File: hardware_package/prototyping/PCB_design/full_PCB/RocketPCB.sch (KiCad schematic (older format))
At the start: 67 parts, among them J1 USB_C_Receptacle, J2 Micro_SD_Card, J3 Conn_01x03_Female, Q1 DMG2301L, SW1 SW_Push, SW2 SW_Push, U1 STM32F405RGTx, U2 TPS62160DSG, U3 RFM69HCW, U4 MPU-6050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

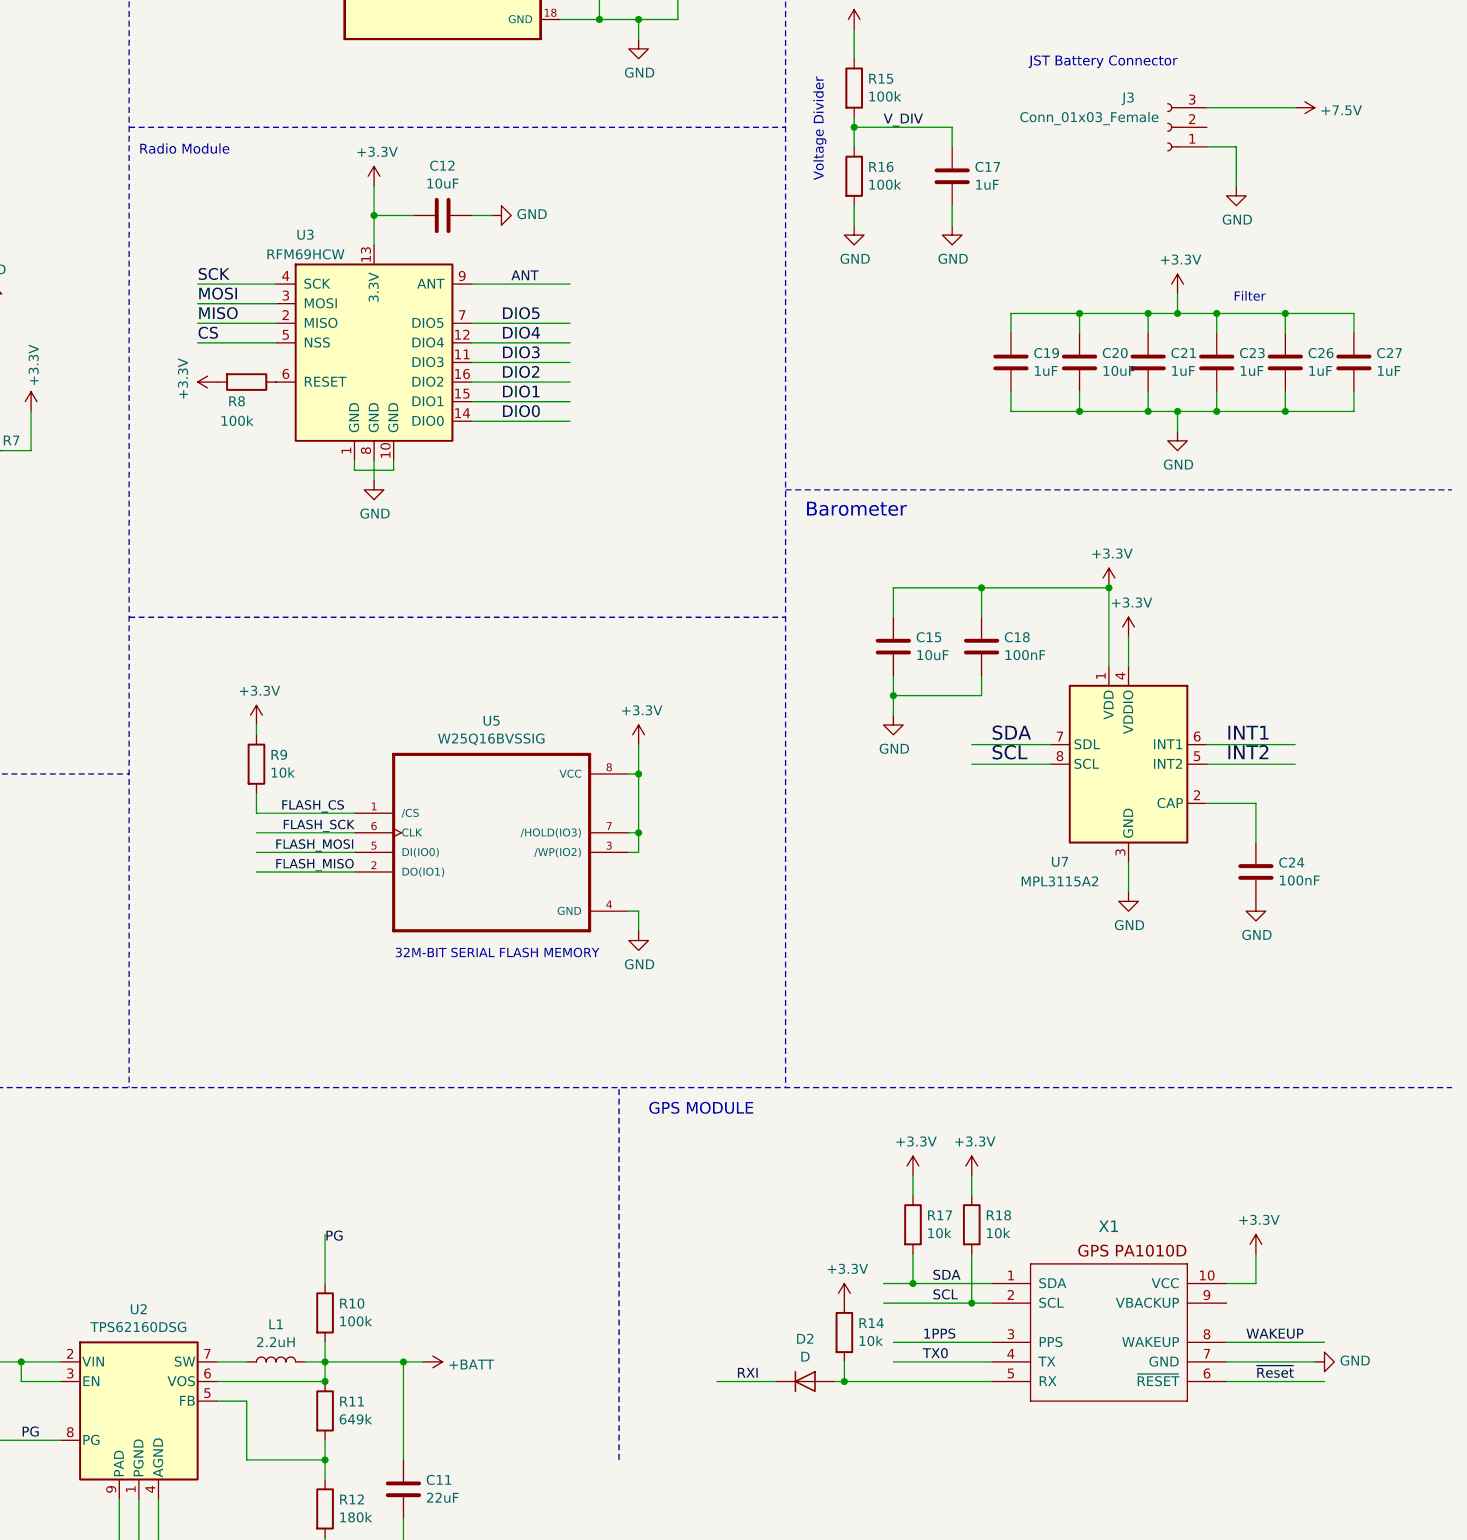
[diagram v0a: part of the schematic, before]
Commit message: Assigned additional footprints adding headers for radio and GPS
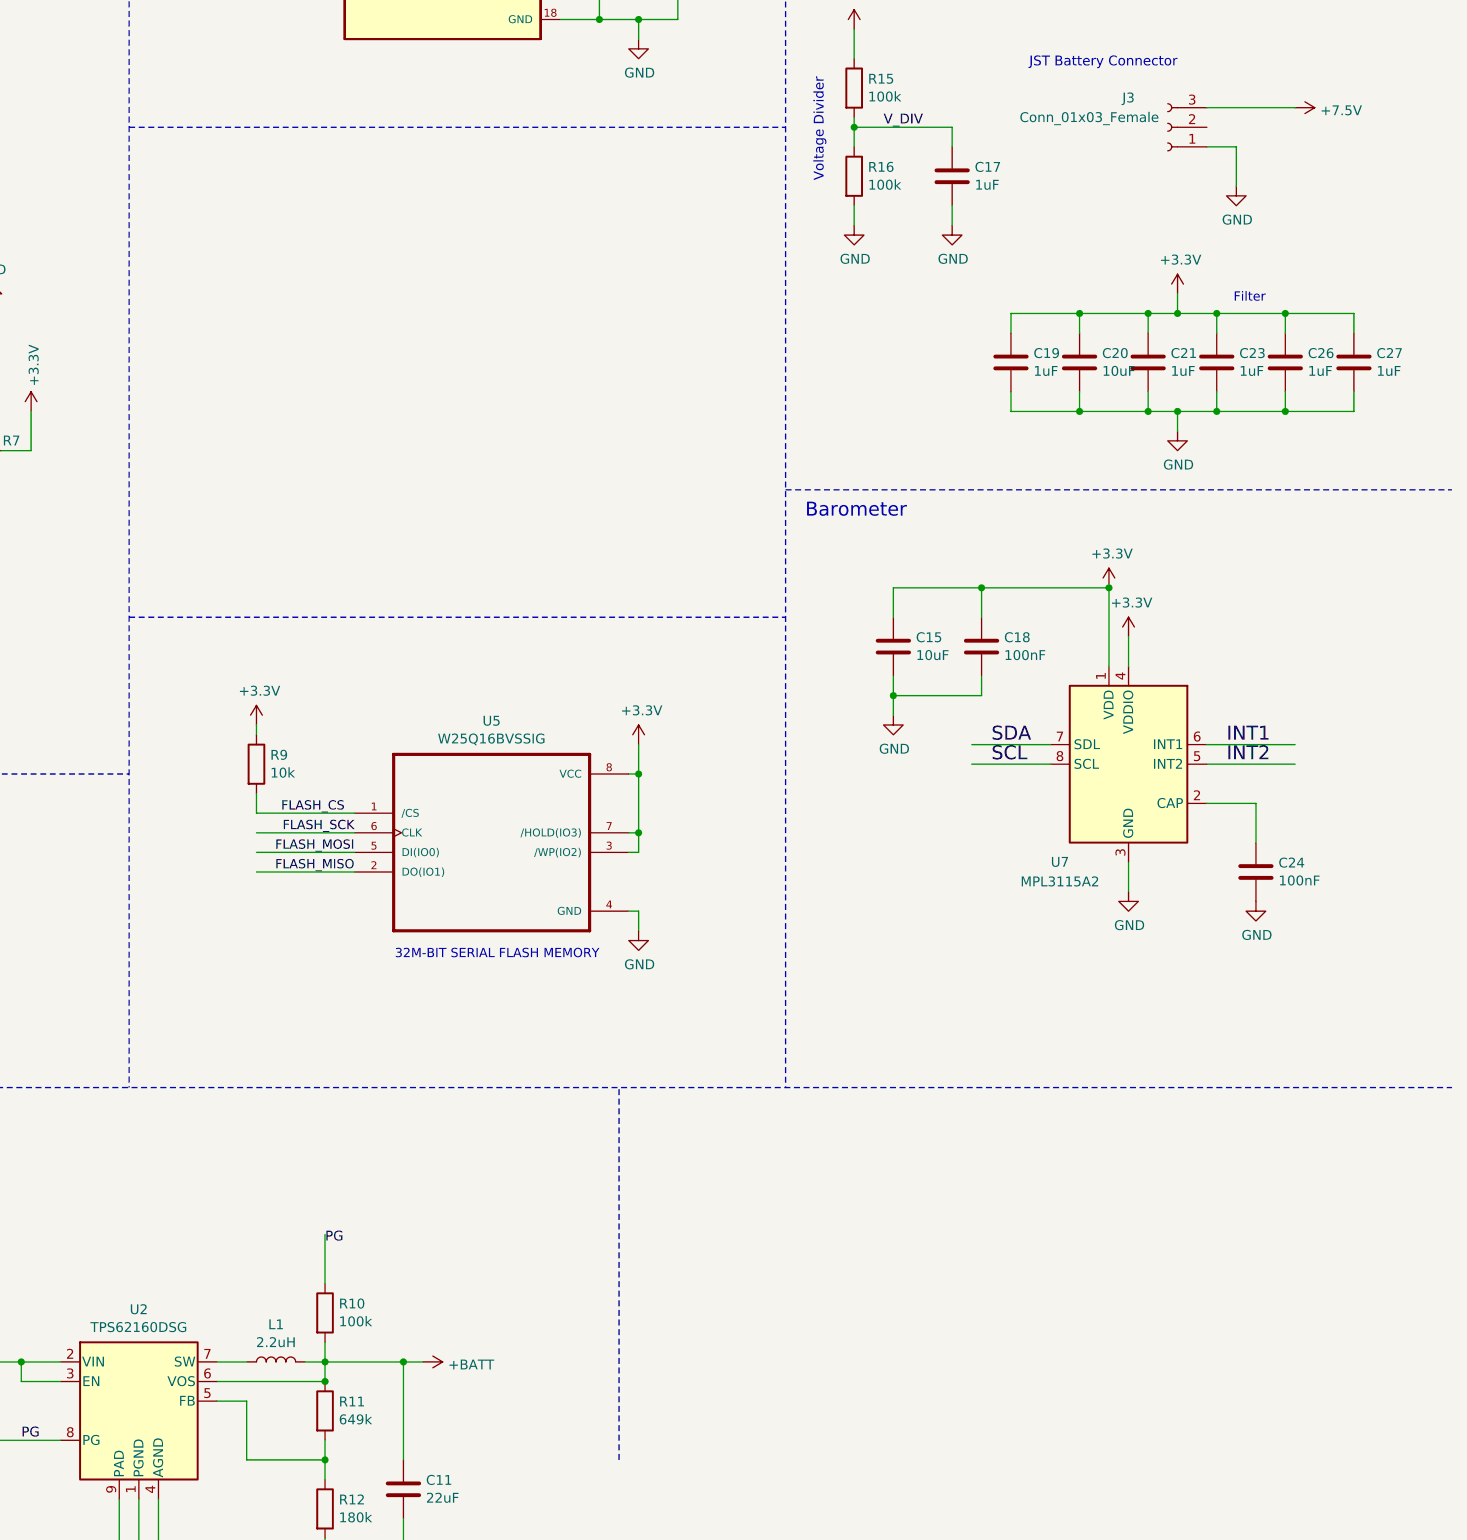
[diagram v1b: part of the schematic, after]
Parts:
- removed C12: 10uF, Capacitor_THT:CP_Radial_D5.0mm_P2.50mm, symbol Device:C
- removed D2: D, LED_THT:LED_D5.0mm_Clear, symbol Device:D
- removed R14, R17, R18: 10k, Resistor_THT:R_Axial_DIN0207_L6.3mm_D2.5mm_P7.62mm_Horizontal, symbol Device:R
- removed R8: 100k, Resistor_THT:R_Axial_DIN0207_L6.3mm_D2.5mm_P7.62mm_Horizontal, symbol Device:R
- removed U3: RFM69HCW, symbol RocketPCB-rescue:RFM69HCW-RF_AM_FM
- removed X1: GPS_PA1010D, symbol RocketPCB-rescue:GPS_PA1010D-gps_pa1010d
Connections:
- net labels removed: 1PPS, ANT, DIO0, DIO1, DIO2, DIO3, DIO4, DIO5, RXI, TX0, WAKEUP, ~Reset~
- wire segments 321 -> 283
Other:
- note removed: "GPS MODULE\n"
- note removed: "Radio Module"

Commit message: Added all FPs some issues still, +safety features and regulator
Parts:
- removed U5: W25Q16BVSSIG, symbol RocketPCB-rescue:W25Q16BVSSIG-W25Q16BVSSIG
- added C12, C28: 10uF, Capacitor_THT:CP_Radial_D5.0mm_P2.50mm, symbol Device:C
- added C29: 0.1uF, Capacitor_THT:CP_Radial_D5.0mm_P2.50mm, symbol Device:C
- added C30: 10pF, Capacitor_THT:CP_Radial_D5.0mm_P2.50mm, symbol Device:C
- added C31, C32, C33: 22uF, Capacitor_THT:CP_Radial_D5.0mm_P2.50mm, symbol Device:C
- added F1: Polyfuse, Fuse:Fuse_Littelfuse_395Series, symbol Device:Polyfuse
- added L2: 1uH, Inductor_THT:L_Axial_L9.5mm_D4.0mm_P12.70mm_Horizontal_Fastron_SMCC, symbol Device:L
- added Q2: Q_PMOS_DGS, Package_TO_SOT_SMD:SOT-23, symbol Device:Q_PMOS_DGS
- added R14: 1M, Resistor_THT:R_Axial_DIN0204_L3.6mm_D1.6mm_P7.62mm_Horizontal, symbol Device:R
- added R8: 2.2M, Resistor_THT:R_Axial_DIN0204_L3.6mm_D1.6mm_P7.62mm_Horizontal, symbol Device:R
- added U3: Radio_Header, GPS_head0:gps_header_footprint, symbol radio_header:Radio_Header
- added U5: W25Q16JV, GPS_head0:W25Q16JV_footprint, symbol flash_memory:W25Q16JV
- added U8: GPS_header, GPS_head0:GPS_header_fp, symbol gps_header:GPS_header
- added U9: TPS63060, Package_SON:Texas_S-PWSON-N10_ThermalVias, symbol Regulator_Switching:TPS63060
- R9: value 10k -> 200k; footprint Resistor_THT:R_Axial_DIN0207_L6.3mm_D2.5mm_P7.62mm_Horizontal -> Resistor_THT:R_Axial_DIN0204_L3.6mm_D1.6mm_P7.62mm_Horizontal
- U4: footprint (none) -> GPS_head0:MPU6050-footprint
- Y1: footprint (none) -> Oscillator:Oscillator_DIP-14_LargePads
- Y2: value 32.768 -> 32MHz; footprint (none) -> Oscillator:Oscillator_DIP-8_LargePads
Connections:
- net labels added: +6V, G0, PPS, RXI, TX0
- wire segments 283 -> 370
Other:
- note added: "16M-BIT SERIAL FLASH MEMORY"
- note added: "3.7V out"
- note added: "FLASH MEMORY\n"
- note added: "GPS Module"
- note added: "Radio Module\n"
- note added: "Voltage Regulator Servos - 6V\n"
- note removed: "32M-BIT SERIAL FLASH MEMORY"
- moved on the sheet: J3

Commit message: Begun laying out PCB
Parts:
- Q2: footprint Package_TO_SOT_SMD:SOT-23 -> (none)
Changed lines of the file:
@@
 Wire Wire Line
 	1650 6900 1850 6900
-Wire Wire Line
-	1650 6900 1050 6900
 Connection ~ 1650 6900
 $Comp
@@
 $EndComp
 $Comp
-L Device:C C12
-U 1 1 5FAE0189
-P 900 7900
-F 0 "C12" H 700 8050 50  0000 L CNN
-F 1 "10uF" H 650 7800 50  0000 L CNN
-F 2 "Capacitor_THT:CP_Radial_D5.0mm_P2.50mm" H 938 7750 50  0001 C CNN
-F 3 "~" H 900 7900 50  0001 C CNN
-	1    900  7900
-	1    0    0    -1
-$EndComp
-$Comp
-L Device:C C28
-U 1 1 5FAE6549
-P 1150 7900
-F 0 "C28" H 1265 7946 50  0000 L CNN
-F 1 "10uF" H 1265 7855 50  0000 L CNN
-F 2 "Capacitor_THT:CP_Radial_D5.0mm_P2.50mm" H 1188 7750 50  0001 C CNN
-F 3 "~" H 1150 7900 50  0001 C CNN
-	1    1150 7900
-	1    0    0    -1
-$EndComp
-Wire Wire Line
-	1050 6900 1050 7550
-Wire Wire Line
-	1050 7550 1150 7550
-Wire Wire Line
-	1150 7550 1150 7750
-Connection ~ 1050 6900
-Wire Wire Line
-	1050 6900 950  6900
-Wire Wire Line
-	1050 7550 900  7550
-Wire Wire Line
-	900  7550 900  7750
-Connection ~ 1050 7550
-$Comp
-L power:GND #PWR0112
-U 1 1 5FB20758
-P 1000 8200
-F 0 "#PWR0112" H 1000 7950 50  0001 C CNN
-F 1 "GND" V 1005 8072 50  0000 R CNN
-F 2 "" H 1000 8200 50  0001 C CNN
-F 3 "" H 1000 8200 50  0001 C CNN
-	1    1000 8200
-	1    0    0    -1
-$EndComp
-Wire Wire Line
-	900  8050 900  8200
-Wire Wire Line
-	900  8200 1000 8200
-Wire Wire Line
-	1000 8200 1150 8200
-Wire Wire Line
-	1150 8200 1150 8050
-Connection ~ 1000 8200
-$Comp
 L Device:C C29
 U 1 1 5FBBFED9
@@
 Wire Wire Line
 	3700 6900 3700 7300
-$Comp
-L Device:C C31
-U 1 1 5FE129F8
-P 4050 7250
-F 0 "C31" H 4165 7296 50  0000 L CNN
-F 1 "22uF" H 4150 7200 50  0000 L CNN
-F 2 "Capacitor_THT:CP_Radial_D5.0mm_P2.50mm" H 4088 7100 50  0001 C CNN
-F 3 "~" H 4050 7250 50  0001 C CNN
-	1    4050 7250
-	1    0    0    -1
-$EndComp
-$Comp
-L Device:C C32
-U 1 1 5FE133D9
-P 4450 7250
-F 0 "C32" H 4565 7296 50  0000 L CNN
-F 1 "22uF" H 4550 7200 50  0000 L CNN
-F 2 "Capacitor_THT:CP_Radial_D5.0mm_P2.50mm" H 4488 7100 50  0001 C CNN
-F 3 "~" H 4450 7250 50  0001 C CNN
-	1    4450 7250
-	1    0    0    -1
-$EndComp
-$Comp
-L Device:C C33
-U 1 1 5FE138A3
-P 4850 7250
-F 0 "C33" H 4965 7296 50  0000 L CNN
-F 1 "22uF" H 4950 7200 50  0000 L CNN
-F 2 "Capacitor_THT:CP_Radial_D5.0mm_P2.50mm" H 4888 7100 50  0001 C CNN
-F 3 "~" H 4850 7250 50  0001 C CNN
-	1    4850 7250
-	1    0    0    -1
-$EndComp
-Wire Wire Line
-	4050 7400 4050 7550
-Wire Wire Line
-	4050 7550 4450 7550
-Wire Wire Line
-	4450 7550 4450 7400
-Wire Wire Line
-	4850 7400 4850 7550
-Wire Wire Line
-	4850 7550 4450 7550
-Connection ~ 4450 7550
-$Comp
-L power:GND #PWR0115
-U 1 1 5FE60576
-P 4450 7650
-F 0 "#PWR0115" H 4450 7400 50  0001 C CNN
-F 1 "GND" V 4455 7522 50  0000 R CNN
-F 2 "" H 4450 7650 50  0001 C CNN
-F 3 "" H 4450 7650 50  0001 C CNN
-	1    4450 7650
-	1    0    0    -1
-$EndComp
-Wire Wire Line
-	4450 7550 4450 7650
 Wire Wire Line
 	3700 6900 4050 6900
-Wire Wire Line
-	4850 6900 4850 7100
 Connection ~ 3700 6900
-Wire Wire Line
-	4450 6900 4450 7100
-Connection ~ 4450 6900
-Wire Wire Line
-	4450 6900 4850 6900
 Wire Wire Line
 	4050 6900 4050 7100
 Connection ~ 4050 6900
 Wire Wire Line
-	4050 6900 4450 6900
-Wire Wire Line
 	2650 6900 3050 6900
 Wire Wire Line
@@
 Wire Wire Line
 	2850 7250 3050 7250
-Wire Wire Line
-	4850 6900 5200 6900
-Connection ~ 4850 6900
 $Comp
 L power:+6V #PWR0116
@@
 Text Notes 600  5400 0    71   ~ 0
 Voltage Regulator Servos - 6V\n
-$Comp
-L Device:Q_PMOS_DGS Q2
-U 1 1 6006F0DB
-P 14950 2650
-F 0 "Q2" V 15292 2650 50  0000 C CNN
-F 1 "Q_PMOS_DGS" V 15201 2650 50  0000 C CNN
-F 2 "Package_TO_SOT_SMD:SOT-23" H 15150 2750 50  0001 C CNN
-F 3 "~" H 14950 2650 50  0001 C CNN
-	1    14950 2650
-	0    -1   -1   0
-$EndComp
 Wire Wire Line
 	14450 2900 14950 2900
@@
 Wire Wire Line
 	15600 2550 15650 2550
+Wire Wire Line
+	4050 7400 4050 7550
+Wire Wire Line
+	4050 7550 4450 7550
+Wire Wire Line
+	4450 7550 4450 7650
+$Comp
+L power:GND #PWR0115
+U 1 1 5FE60576
+P 4450 7650
+F 0 "#PWR0115" H 4450 7400 50  0001 C CNN
+F 1 "GND" V 4455 7522 50  0000 R CNN
+F 2 "" H 4450 7650 50  0001 C CNN
+F 3 "" H 4450 7650 50  0001 C CNN
+	1    4450 7650
+	1    0    0    -1
+$EndComp
+$Comp
+L Device:C C31
+U 1 1 5FE129F8
+P 4050 7250
+F 0 "C31" H 4165 7296 50  0000 L CNN
+F 1 "22uF" H 4150 7200 50  0000 L CNN
+F 2 "Capacitor_THT:CP_Radial_D5.0mm_P2.50mm" H 4088 7100 50  0001 C CNN
+F 3 "~" H 4050 7250 50  0001 C CNN
+	1    4050 7250
+	1    0    0    -1
+$EndComp
+Wire Wire Line
+	4050 6900 4450 6900
+Connection ~ 4450 6900
+Wire Wire Line
+	4450 6900 4450 7100
+Connection ~ 4450 7550
+Wire Wire Line
+	4450 7550 4450 7400
+Wire Wire Line
+	4850 7550 4450 7550
+Wire Wire Line
+	4850 6900 5200 6900
+Wire Wire Line
+	4450 6900 4850 6900
+Connection ~ 4850 6900
+Wire Wire Line
+	4850 6900 4850 7100
+Wire Wire Line
+	4850 7400 4850 7550
+$Comp
+L Device:C C33
+U 1 1 5FE138A3
+P 4850 7250
+F 0 "C33" H 4965 7296 50  0000 L CNN
+F 1 "22uF" H 4950 7200 50  0000 L CNN
+F 2 "Capacitor_THT:CP_Radial_D5.0mm_P2.50mm" H 4888 7100 50  0001 C CNN
+F 3 "~" H 4850 7250 50  0001 C CNN
+	1    4850 7250
+	1    0    0    -1
+$EndComp
+$Comp
+L Device:C C32
+U 1 1 5FE133D9
+P 4450 7250
+F 0 "C32" H 4565 7296 50  0000 L CNN
+F 1 "22uF" H 4550 7200 50  0000 L CNN
+F 2 "Capacitor_THT:CP_Radial_D5.0mm_P2.50mm" H 4488 7100 50  0001 C CNN
+F 3 "~" H 4450 7250 50  0001 C CNN
+	1    4450 7250
+	1    0    0    -1
+$EndComp
+Wire Wire Line
+	1050 6900 950  6900
+Wire Wire Line
+	1650 6900 1050 6900
+Connection ~ 1050 6900
+Wire Wire Line
+	1050 6900 1050 7550
+$Comp
+L power:GND #PWR0112
+U 1 1 5FB20758
+P 1000 8200
+F 0 "#PWR0112" H 1000 7950 50  0001 C CNN
+F 1 "GND" V 1005 8072 50  0000 R CNN
+F 2 "" H 1000 8200 50  0001 C CNN
+F 3 "" H 1000 8200 50  0001 C CNN
+	1    1000 8200
+	1    0    0    -1
+$EndComp
+Wire Wire Line
+	1000 8200 1150 8200
+Wire Wire Line
+	1150 8200 1150 8050
+Wire Wire Line
+	1050 7550 1150 7550
+Wire Wire Line
+	1150 7550 1150 7750
+$Comp
+L Device:C C28
+U 1 1 5FAE6549
+P 1150 7900
+F 0 "C28" H 1265 7946 50  0000 L CNN
+F 1 "10uF" H 1265 7855 50  0000 L CNN
+F 2 "Capacitor_THT:CP_Radial_D5.0mm_P2.50mm" H 1188 7750 50  0001 C CNN
+F 3 "~" H 1150 7900 50  0001 C CNN
+	1    1150 7900
+	1    0    0    -1
+$EndComp
+Connection ~ 1000 8200
+Wire Wire Line
+	900  8200 1000 8200
+Connection ~ 1050 7550
+Wire Wire Line
+	1050 7550 900  7550
+Wire Wire Line
+	900  7550 900  7750
+Wire Wire Line
+	900  8050 900  8200
+$Comp
+L Device:C C12
+U 1 1 5FAE0189
+P 900 7900
+F 0 "C12" H 700 8050 50  0000 L CNN
+F 1 "10uF" H 650 7800 50  0000 L CNN
+F 2 "Capacitor_THT:CP_Radial_D5.0mm_P2.50mm" H 938 7750 50  0001 C CNN
+F 3 "~" H 900 7900 50  0001 C CNN
+	1    900  7900
+	1    0    0    -1
+$EndComp
+$Comp
+L Device:Q_PMOS_DGS Q2
+U 1 1 6006F0DB
+P 14950 2650
+F 0 "Q2" V 15292 2650 50  0000 C CNN
+F 1 "Q_PMOS_DGS" V 15201 2650 50  0000 C CNN
+F 2 "" H 15150 2750 50  0001 C CNN
+F 3 "~" H 14950 2650 50  0001 C CNN
+	1    14950 2650
+	0    -1   -1   0
+$EndComp
 $EndSCHEMATC
